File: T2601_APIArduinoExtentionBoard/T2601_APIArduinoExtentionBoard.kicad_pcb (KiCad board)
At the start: 2 copper layers, 60 x 90 mm, 90 parts, among them J1 Conn_01x10_Socket, J11 Conn_01x04_Pin, J12 Screw_Terminal_01x02, J13 Conn_01x04_Pin, J14 Screw_Terminal_01x02, J15 Conn_02x08_Counter_Clockwise, J2 Conn_01x10_Socket, J3 Conn_01x10_Socket, J4 Conn_01x10_Socket, J5 Screw_Terminal_01x08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

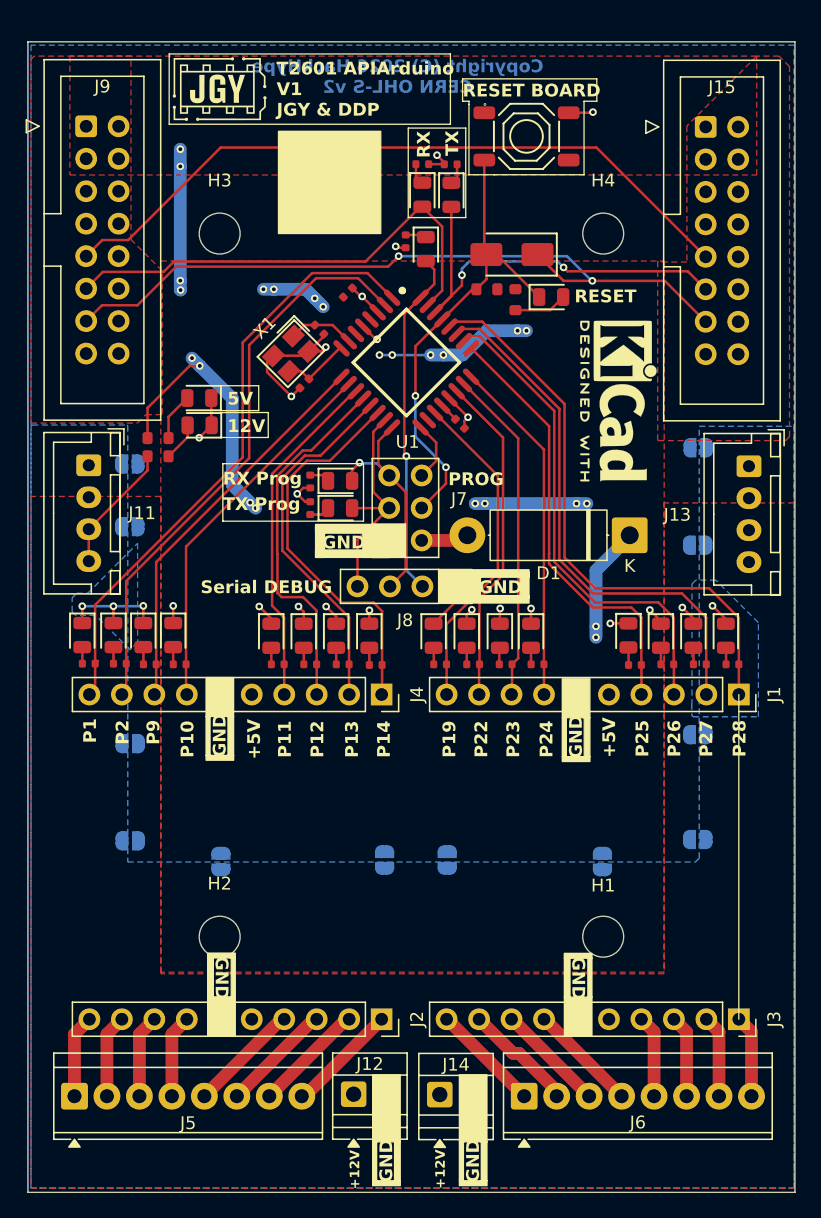
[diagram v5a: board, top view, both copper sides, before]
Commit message: Side Tolerances + Resistor Value
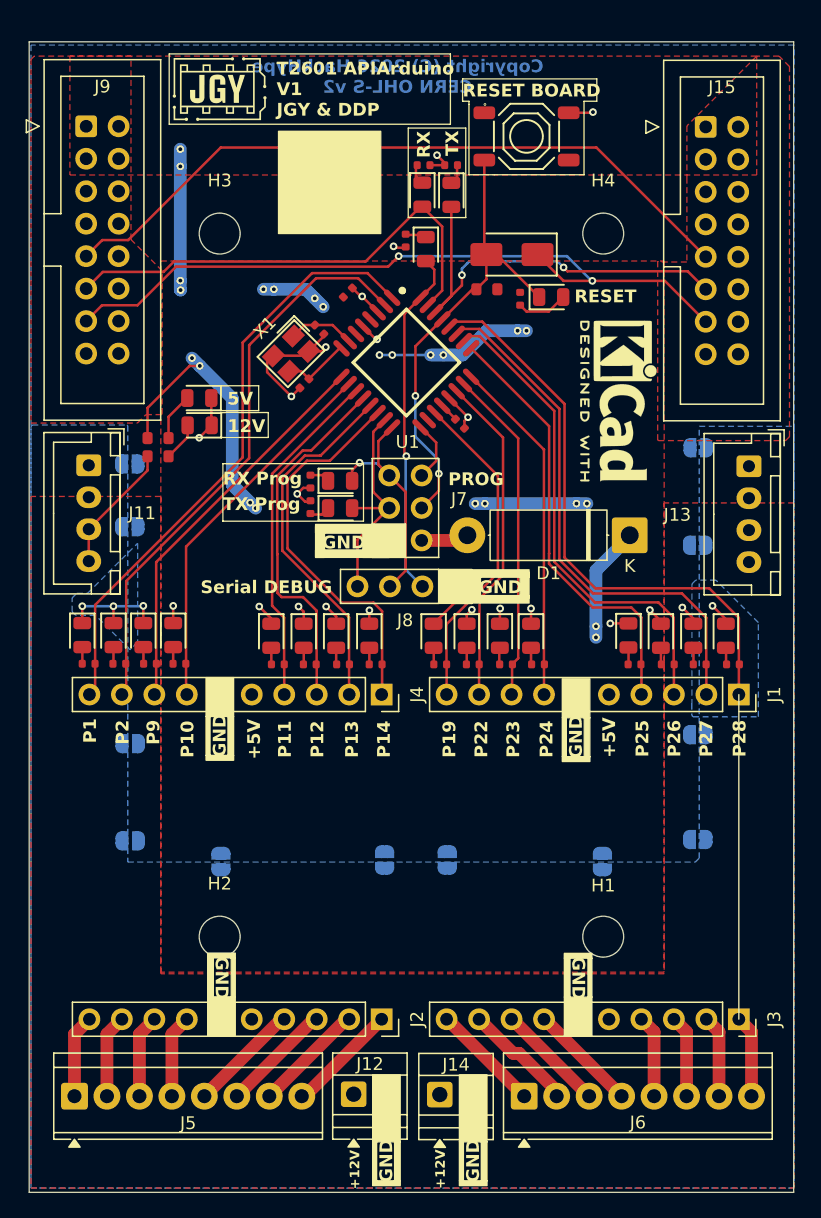
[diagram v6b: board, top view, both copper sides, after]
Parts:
- R1, R10, R11, R12, R13, R14, R15, R16, R17, R18, R19, R2, R20, R21, R22, R3, R4, R6, R7, R8, R9: value 510Ω -> 1kΩ
- R25: footprint PCM_JLCPCB:R_0603 -> PCM_JLCPCB:R_0402
- moved R3 44.5 mm to (156.9, 41.6), turned to 0 degrees
- moved R4 44.4 mm to (159.1, 41.6)
- moved R10 43.5 mm to (137.8, 80.7), turned to 180 degrees
- moved R11 41.4 mm to (145.6, 80.7)
- moved R2 39.9 mm to (155.6, 47.5), turned to -90 degrees
- moved R12 33.9 mm to (148.1, 80.7), turned to 180 degrees
- moved R22 22.9 mm to (181.2, 80.7)
- moved R15 22.9 mm to (158.2, 80.7)
- moved R8 19.3 mm to (133.1, 80.7), turned to 180 degrees
- moved R9 19.0 mm to (135.6, 80.7), turned to 180 degrees
- moved R16 17.8 mm to (160.8, 80.7)
- moved R21 17.7 mm to (178.6, 80.7)
- moved R6 14.5 mm to (148.1, 66.4), turned to -90 degrees
- moved R20 12.7 mm to (176.1, 80.7)
- moved R17 12.6 mm to (163.4, 80.7)
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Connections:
- R10 pad 1: Net-(D11-Pad1) -> P10
- R10 pad 2: GND -> Net-(D14-Pad2)
- R11 pad 1: Net-(D12-Pad1) -> P11
- R11 pad 2: GND -> Net-(D15-Pad2)
- R12 pad 1: Net-(D13-Pad1) -> P12
- R12 pad 2: GND -> Net-(D16-Pad2)
- R15 pad 1: P28 -> P19
- R15 pad 2: Net-(D25-Pad2) -> Net-(D2-Pad2)
- R16 pad 1: P27 -> P22
- R16 pad 2: Net-(D24-Pad2) -> Net-(D19-Pad2)
- R17 pad 1: P26 -> P23
- R17 pad 2: Net-(D23-Pad2) -> Net-(D20-Pad2)
- R18 pad 1: P25 -> P24
- R18 pad 2: Net-(D22-Pad2) -> Net-(D21-Pad2)
- R19 pad 1: P24 -> P25
- R19 pad 2: Net-(D21-Pad2) -> Net-(D22-Pad2)
- R2 pad 1: P2 -> Net-(D13-Pad1)
- R2 pad 2: Net-(D4-Pad2) -> GND
- R20 pad 1: P23 -> P26
- R20 pad 2: Net-(D20-Pad2) -> Net-(D23-Pad2)
- R21 pad 1: P22 -> P27
- R21 pad 2: Net-(D19-Pad2) -> Net-(D24-Pad2)
- R22 pad 1: P19 -> P28
- R22 pad 2: Net-(D2-Pad2) -> Net-(D25-Pad2)
- R3 pad 1: P9 -> Net-(D11-Pad1)
- R3 pad 2: Net-(D5-Pad2) -> GND
- R4 pad 1: P10 -> Net-(D12-Pad1)
- R4 pad 2: Net-(D14-Pad2) -> GND
- R6 pad 1: P11 -> Net-(D10-Pad1)
- R6 pad 2: Net-(D15-Pad2) -> GND
- R7 pad 1: P12 -> Net-(D9-Pad1)
- R7 pad 2: Net-(D16-Pad2) -> GND
- R8 pad 1: Net-(D9-Pad1) -> P2
- R8 pad 2: GND -> Net-(D4-Pad2)
- R9 pad 1: Net-(D10-Pad1) -> P9
- R9 pad 2: GND -> Net-(D5-Pad2)
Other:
- board size 60 x 90 mm -> 59.8 x 90 mm

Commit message: Capacitor + plane correction
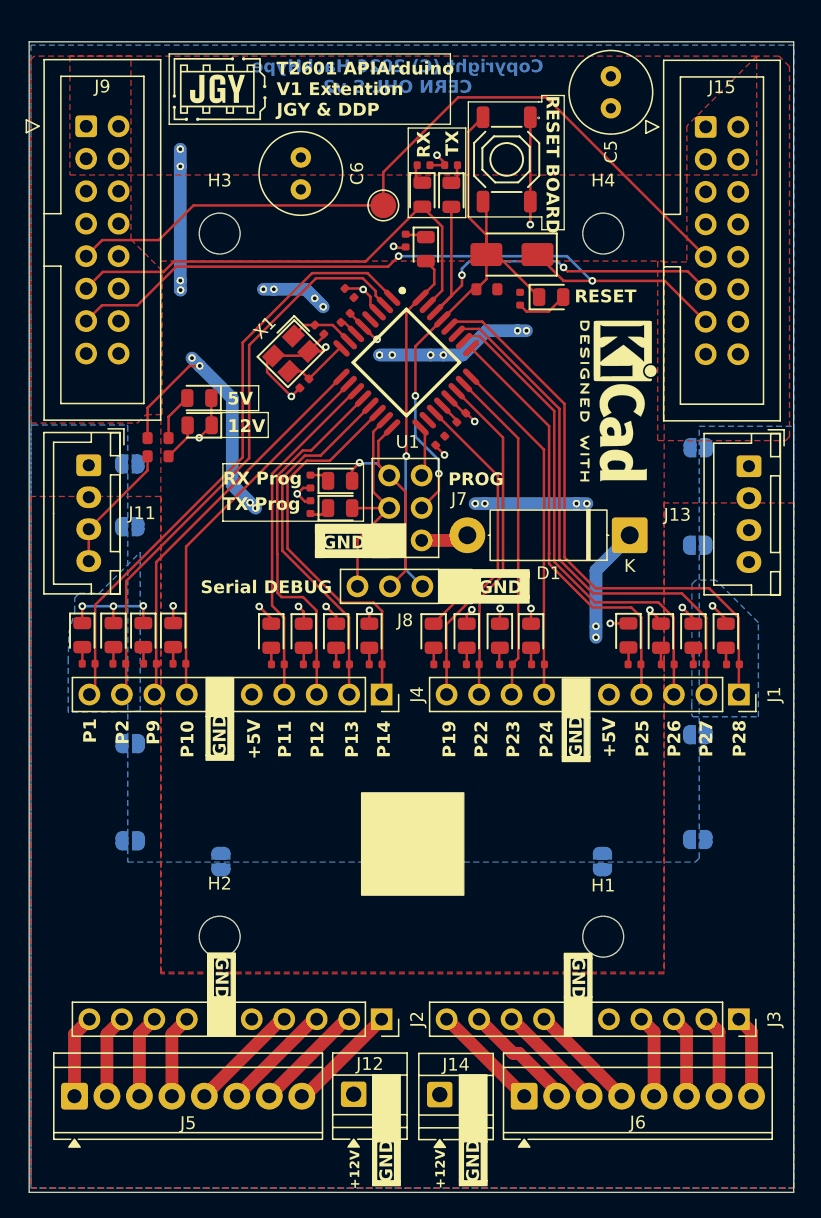
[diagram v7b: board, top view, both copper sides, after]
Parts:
- added C5: C, Capacitor_THT:C_Radial_D6.3mm_H11.0mm_P2.50mm, F.Cu at (171.6, 34.7)
- added C6: C, Capacitor_THT:C_Radial_D6.3mm_H11.0mm_P2.50mm, F.Cu at (147.3, 41.0)
- added C7: 100nF, PCM_JLCPCB:C_0402, F.Cu at (150.8, 53.6)
- added C8: 100nF, PCM_JLCPCB:C_0402, F.Cu at (158.2, 63.2)
- added TP1: TestPoint, TestPoint:TestPoint_Pad_D2.0mm, F.Cu at (153.8, 44.8)
- moved S1 2.38 mm to (163.4, 41.2), turned to -90 degrees
- moved C4 0.49 mm to (159.9, 61.4), turned to 45 degrees
- moved C3 0.13 mm to (151.2, 51.6), turned to 135 degrees
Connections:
- S1 pad 1: unconnected-(S1-A-Pad1) -> GND
- S1 pad 4: unconnected-(S1-D-Pad4) -> RESET
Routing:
- net GND: track 59.6 -> 69.3 mm, vias 25 -> 26
- net RESET: track 36.7 -> 45.5 mm
- net UART_BACK: track 55.9 -> 60.7 mm
- net +5V: track 68.0 -> 69.5 mm
- net SCK: track 4.76 -> 4.03 mm
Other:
- board text added: "T2601 APIArduino V1 Extention JGY & DDP"
- board text removed: "T2601 APIArduino V1 JGY & DDP"

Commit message: Move C3
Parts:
- moved C3 1.25 mm to (152.3, 52.2), turned to 45 degrees
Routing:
- net GND: track 69.3 -> 68.1 mm
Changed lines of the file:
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@@
 	(footprint "PCM_JLCPCB:C_0402"
 		(layer "F.Cu")
-		(at 151.15 51.65 135)
+		(at 152.273 52.197 45)
 		(descr "Capacitor SMD 0402 (1005 Metric), square (rectangular) end terminal, IPC_7351 nominal, (Body size source: IPC-SM-782 page 76, https://www.pcb-3d.com/wordpress/wp-content/uploads/ipc-sm-782a_amendment_1_and_2.pdf), generated with kicad-footprint-generator")
 		(tags "capacitor")
 		(property "Reference" "C3"
-			(at 0 -1.16 135)
+			(at 0 -1.16 45)
 			(layer "F.SilkS")
 			(hide yes)
@@
 		)
 		(property "Value" "100nF"
-			(at 0 1.16 135)
+			(at 0 1.16 45)
 			(layer "F.Fab")
 			(effects
@@
 		)
 		(property "Datasheet" "https://www.lcsc.com/datasheet/lcsc_datasheet_2304140030_Samsung-Electro-Mechanics-CL05B104KO5NNNC_C1525.pdf"
-			(at 0 0 135)
+			(at 0 0 45)
 			(unlocked yes)
 			(layer "F.Fab")
@@
 		)
 		(property "Description" "16V 100nF X7R ±10% 0402 Multilayer Ceramic Capacitors MLCC - SMD/SMT ROHS"
-			(at 0 0 135)
+			(at 0 0 45)
 			(unlocked yes)
 			(layer "F.Fab")
@@
 		)
 		(property "LCSC" "C1525"
-			(at 0 0 135)
+			(at 0 0 45)
 			(unlocked yes)
 			(layer "F.Fab")
@@
 		)
 		(property "Stock" "20208285"
-			(at 0 0 135)
+			(at 0 0 45)
 			(unlocked yes)
 			(layer "F.Fab")
@@
 		)
 		(property "Price" "0.004USD"
-			(at 0 0 135)
+			(at 0 0 45)
 			(unlocked yes)
 			(layer "F.Fab")
@@
 		)
 		(property "Process" "SMT"
-			(at 0 0 135)
+			(at 0 0 45)
 			(unlocked yes)
 			(layer "F.Fab")
@@
 		)
 		(property "Minimum Qty" "20"
-			(at 0 0 135)
+			(at 0 0 45)
 			(unlocked yes)
 			(layer "F.Fab")
@@
 		)
 		(property "Attrition Qty" "10"
-			(at 0 0 135)
+			(at 0 0 45)
 			(unlocked yes)
 			(layer "F.Fab")
@@
 		)
 		(property "Class" "Basic Component"
-			(at 0 0 135)
+			(at 0 0 45)
 			(unlocked yes)
 			(layer "F.Fab")
@@
 		)
 		(property "Category" "Capacitors,Multilayer Ceramic Capacitors MLCC - SMD/SMT"
-			(at 0 0 135)
+			(at 0 0 45)
 			(unlocked yes)
 			(layer "F.Fab")
@@
 		)
 		(property "Manufacturer" "Samsung Electro-Mechanics"
-			(at 0 0 135)
+			(at 0 0 45)
 			(unlocked yes)
 			(layer "F.Fab")
@@
 		)
 		(property "Part" "CL05B104KO5NNNC"
-			(at 0 0 135)
+			(at 0 0 45)
 			(unlocked yes)
 			(layer "F.Fab")
@@
 		)
 		(property "Voltage Rated" "16V"
-			(at 0 0 135)
+			(at 0 0 45)
 			(unlocked yes)
 			(layer "F.Fab")
@@
 		)
 		(property "Tolerance" "±10%"
-			(at 0 0 135)
+			(at 0 0 45)
 			(unlocked yes)
 			(layer "F.Fab")
@@
 		)
 		(property "Capacitance" "100nF"
-			(at 0 0 135)
+			(at 0 0 45)
 			(unlocked yes)
 			(layer "F.Fab")
@@
 		)
 		(property "Temperature Coefficient" "X7R"
-			(at 0 0 135)
+			(at 0 0 45)
 			(unlocked yes)
 			(layer "F.Fab")
@@
 		(attr smd)
 		(fp_line
-			(start 0.9 -0.4)
-			(end 0.9 0.4)
+			(start -0.9 -0.4)
+			(end -0.9 0.4)
 			(stroke
 				(width 0.05)
@@
 		)
 		(fp_line
-			(start 0.9 0.4)
-			(end -0.9 0.4)
+			(start -0.9 -0.4)
+			(end 0.9 -0.4)
 			(stroke
 				(width 0.05)
@@
 		)
 		(fp_line
-			(start -0.9 -0.4)
-			(end 0.9 -0.4)
+			(start 0.9 -0.4)
+			(end 0.9 0.4)
 			(stroke
 				(width 0.05)
@@
 		)
 		(fp_line
-			(start -0.9 -0.4)
+			(start 0.9 0.4)
 			(end -0.9 0.4)
 			(stroke
@@
 		)
 		(fp_line
-			(start 0.5 -0.25)
-			(end 0.5 0.25)
+			(start -0.5 -0.25)
+			(end 0.5 -0.25)
 			(stroke
 				(width 0.1)
@@
 		)
 		(fp_line
-			(start 0.5 0.25)
-			(end -0.5 0.25)
+			(start -0.5 0.25)
+			(end -0.5 -0.25)
 			(stroke
 				(width 0.1)
@@
 		)
 		(fp_line
-			(start -0.5 -0.25)
-			(end 0.5 -0.25)
+			(start 0.5 -0.25)
+			(end 0.5 0.25)
 			(stroke
 				(width 0.1)
@@
 		)
 		(fp_line
-			(start -0.5 0.25)
-			(end -0.5 -0.25)
+			(start 0.5 0.25)
+			(end -0.5 0.25)
 			(stroke
 				(width 0.1)
@@
 		)
 		(fp_text user "${REFERENCE}"
-			(at 0 0 135)
+			(at 0 0 45)
 			(layer "F.Fab")
 			(effects
@@
 		)
 		(pad "1" smd roundrect
-			(at -0.499999 0 135)
+			(at -0.499999 0 45)
 			(size 0.56 0.62)
 			(layers "F.Cu" "F.Mask" "F.Paste")
@@
 		)
 		(pad "2" smd roundrect
-			(at 0.499999 0 135)
+			(at 0.499999 0 45)
 			(size 0.56 0.62)
 			(layers "F.Cu" "F.Mask" "F.Paste")
@@
 	)
 	(segment
-		(start 152.225735 51.374265)
-		(end 152.147917 51.296447)
-		(width 0.2)
-		(layer "F.Cu")
-		(net 2)
-	)
-	(segment
 		(start 154.6 48)
 		(end 154.765783 48)
@@
 	)
 	(segment
-		(start 152.799 52.593978)
-		(end 152.799 51.94753)
-		(width 0.2)
-		(layer "F.Cu")
-		(net 2)
-	)
-	(segment
 		(start 160.296447 61.046447)
 		(end 160.95 61.7)
@@
 	)
 	(segment
+		(start 152.019 51.181)
+		(end 152.019 51.235894)
+		(width 0.2)
+		(layer "F.Cu")
+		(net 2)
+	)
+	(segment
 		(start 180.594 77.1652)
 		(end 179.5526 76.1238)
@@
 	)
 	(segment
-		(start 152.147917 51.296447)
-		(end 150.796447 51.296447)
-		(width 0.2)
-		(layer "F.Cu")
-		(net 2)
-	)
-	(segment
 		(start 162.9156 76.3524)
 		(end 162.941 76.327)
@@
 	)
 	(segment
+		(start 152.626553 51.843447)
+		(end 152.626553 52.421531)
+		(width 0.2)
+		(layer "F.Cu")
+		(net 2)
+	)
+	(segment
 		(start 148.082 66.895599)
 		(end 147.531201 66.895599)
@@
 	)
 	(segment
-		(start 153.358872 53.15385)
-		(end 152.799 52.593978)
-		(width 0.2)
-		(layer "F.Cu")
-		(net 2)
-	)
-	(segment
 		(start 147.627885 56.553877)
 		(end 145.223723 56.553877)
@@
 	)
 	(segment
-		(start 152.799 51.94753)
-		(end 152.225735 51.374265)
-		(width 0.2)
-		(layer "F.Cu")
-		(net 2)
-	)
-	(segment
 		(start 147.574 77.520601)
 		(end 147.574 76.581)
@@
 	)
 	(segment
+		(start 152.019 51.235894)
+		(end 152.626553 51.843447)
+		(width 0.2)
+		(layer "F.Cu")
+		(net 2)
+	)
+	(segment
 		(start 172.974 77.495002)
 		(end 171.551998 77.495002)
@@
 	)
 	(segment
+		(start 152.626553 52.421531)
+		(end 153.358872 53.15385)
+		(width 0.2)
+		(layer "F.Cu")
+		(net 2)
+	)
+	(segment
 		(start 165.3 44.5)
 		(end 165.3 46.3)
@@
 	)
 	(via
-		(at 152.225735 51.374265)
+		(at 152.019 51.181)
 		(size 0.6)
 		(drill 0.3)
